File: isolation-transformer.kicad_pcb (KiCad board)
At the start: 2 copper layers, 152.1 x 85.4 mm, 59 parts, among them J1 MODE, J10 PWR, J2 MG950-9.5, J3 MG950-9.5, J4 MG950-9.5, J5 MG950-9.5, J6 MG950-9.5, J7 PWR, J8 MG950-9.5, J9 MG950-9.5, K1 Fujitsu_FTR-F1C, K2 Fujitsu_FTR-F1C, K3 Fujitsu_FTR-F1C, K4 Fujitsu_FTR-F1C, K5 Fujitsu_FTR-F1C, K6 Fujitsu_FTR-F1C, Q1 BC546, Q2 BC546, Q3 BC546, Q4 BC546, Q5 BC546, Q6 BC546, U1 HEF4093B, U2 NE555, U3 LM7805_TO220, U4 7400, U5 NE555, U6 NE555

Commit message: Fixes in mode selection logic
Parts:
- R4: value 4.7k -> 3k
- R7: value 1k -> 10
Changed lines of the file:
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@@
       (effects (font (size 1 1) (thickness 0.15)))
     )
-    (fp_text value 1k (at 1.27 2.37 90) (layer F.Fab)
+    (fp_text value 10 (at 1.27 2.37 90) (layer F.Fab)
       (effects (font (size 1 1) (thickness 0.15)))
     )
@@
       (effects (font (size 1 1) (thickness 0.15)))
     )
-    (fp_text value 4.7k (at 1.27 2.37) (layer F.Fab)
-      (effects (font (size 1 1) (thickness 0.15)))
-    )
+    (fp_text value 3k (at 1.27 2.37) (layer F.Fab)
+      (effects (font (size 1 1) (thickness 0.15)))
+    )

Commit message: Fix relay firing order in soft-start
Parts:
- R11: value 22k -> 10k
- R13: value 10k -> 22k
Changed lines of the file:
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@@
       (effects (font (size 1 1) (thickness 0.15)))
     )
-    (fp_text value 22k (at 1.27 2.37) (layer F.Fab)
+    (fp_text value 10k (at 1.27 2.37) (layer F.Fab)
       (effects (font (size 1 1) (thickness 0.15)))
     )
@@
       (effects (font (size 1 1) (thickness 0.15)))
     )
-    (fp_text value 10k (at 1.27 2.37 180) (layer F.Fab)
+    (fp_text value 22k (at 1.27 2.37 180) (layer F.Fab)
       (effects (font (size 1 1) (thickness 0.15)))
     )

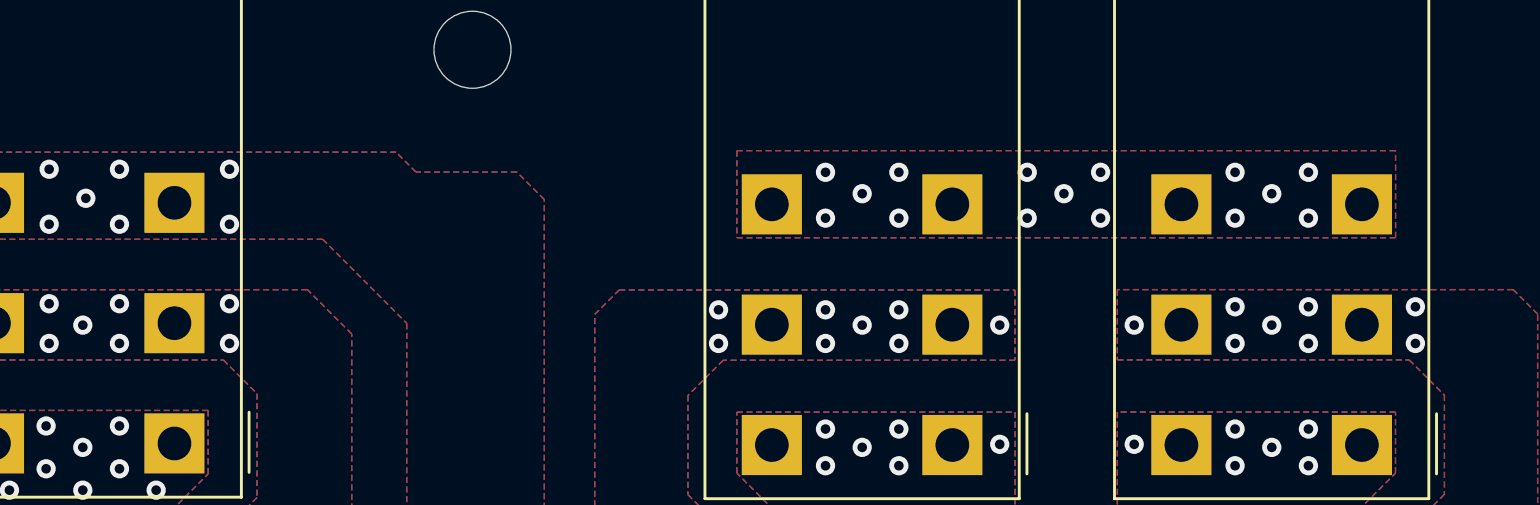
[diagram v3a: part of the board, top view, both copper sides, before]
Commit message: Actually used parts instead of generic ones
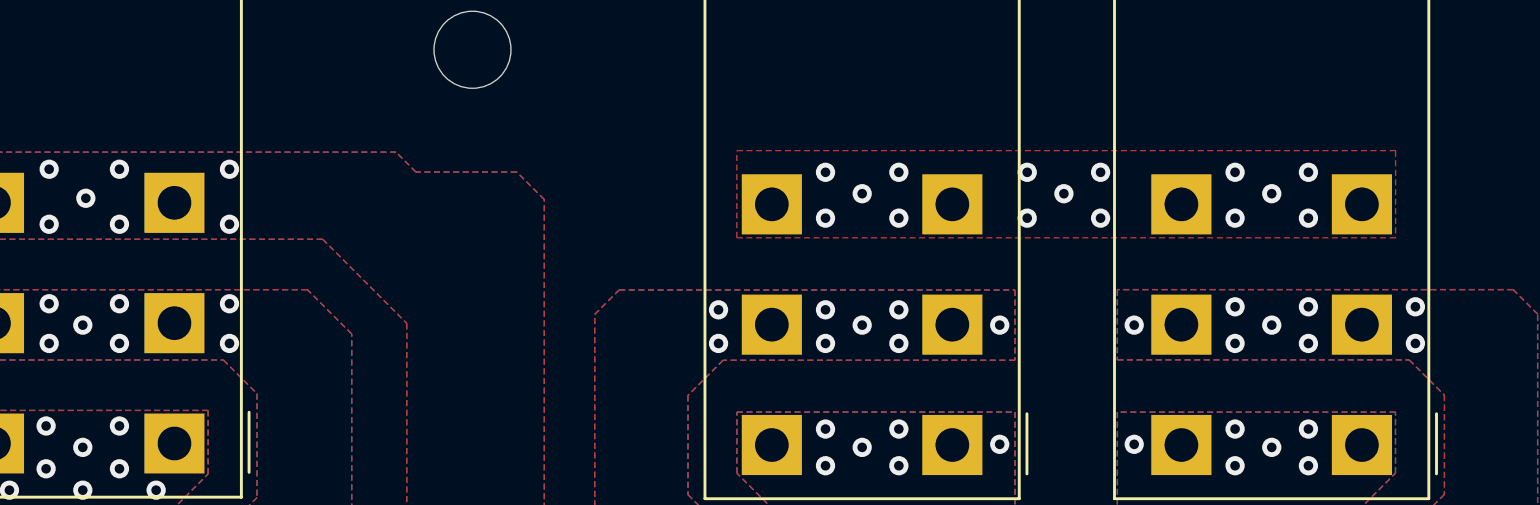
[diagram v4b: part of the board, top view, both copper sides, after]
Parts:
- K1: value Fujitsu_FTR-F1C -> G2R-1-E-12VDC
- K2, K3, K4: value Fujitsu_FTR-F1C -> G2R-1-E-12VDC; footprint Relay_THT:Relay_DPDT_Fujitsu_FTR-F1C -> CustomParts:Relay_SPDT_Omron_G2R-1-E
- K5, K6: value Fujitsu_FTR-F1C -> FTR-K1CK012W
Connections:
- K1 pad 1: /Mode Selection/115V_1_L -> Net-(D1-Pad2)
- K1 pad 2: /Mode Selection/W5 -> /Mode Selection/230V_L
- K1 pad 3: /Mode Selection/230V_L -> /Mode Selection/W5
- K1 pad 4: Net-(D1-Pad2) -> /Mode Selection/115V_1_L
- K1 pad 5: +12V -> /Mode Selection/115V_1_L
- K1 pad 6: /Mode Selection/230V_L -> /Mode Selection/W5
- K1 pad 7: /Mode Selection/W5 -> /Mode Selection/230V_L
- K1 pad 8: /Mode Selection/115V_1_L -> +12V
- K2 pad 1: /Mode Selection/115V_1_N -> Net-(D2-Pad2)
- K2 pad 2: /Mode Selection/W6 -> Net-(K2-Pad2)
- K2 pad 3: Net-(K2-Pad3) -> /Mode Selection/W6
- K2 pad 4: Net-(D2-Pad2) -> /Mode Selection/115V_1_N
- K2 pad 5: +12V -> /Mode Selection/115V_1_N
- K2 pad 6: Net-(K2-Pad3) -> /Mode Selection/W6
- K2 pad 7: /Mode Selection/W6 -> Net-(K2-Pad2)
- K2 pad 8: /Mode Selection/115V_1_N -> +12V
- K3 pad 1: /Mode Selection/115V_2_L -> +12V
- K3 pad 2: /Mode Selection/W7 -> Net-(K2-Pad2)
- K3 pad 3: Net-(K2-Pad3) -> /Mode Selection/W7
- K3 pad 4: +12V -> /Mode Selection/115V_2_L
- K3 pad 5: Net-(D3-Pad2) -> /Mode Selection/115V_2_L
- K3 pad 6: Net-(K2-Pad3) -> /Mode Selection/W7
- K3 pad 7: /Mode Selection/W7 -> Net-(K2-Pad2)
- K3 pad 8: /Mode Selection/115V_2_L -> Net-(D3-Pad2)
- K4 pad 1: /Mode Selection/115V_2_N -> Net-(D4-Pad2)
- K4 pad 2: /Mode Selection/W8 -> /Mode Selection/230V_N
- K4 pad 3: /Mode Selection/230V_N -> /Mode Selection/W8
- K4 pad 4: Net-(D4-Pad2) -> /Mode Selection/115V_2_N
- K4 pad 5: +12V -> /Mode Selection/115V_2_N
- K4 pad 6: /Mode Selection/230V_N -> /Mode Selection/W8
- K4 pad 7: /Mode Selection/W8 -> /Mode Selection/230V_N
- K4 pad 8: /Mode Selection/115V_2_N -> +12V
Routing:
- net Net-(K2-Pad3): vias 15 -> 0
- net Net-(K2-Pad2): vias 0 -> 15
- added copper zone on F.Cu, net Net-(K2-Pad2)
- removed copper zone on B.Cu, net Net-(K2-Pad3)
- removed copper zone on F.Cu, net Net-(K2-Pad3)

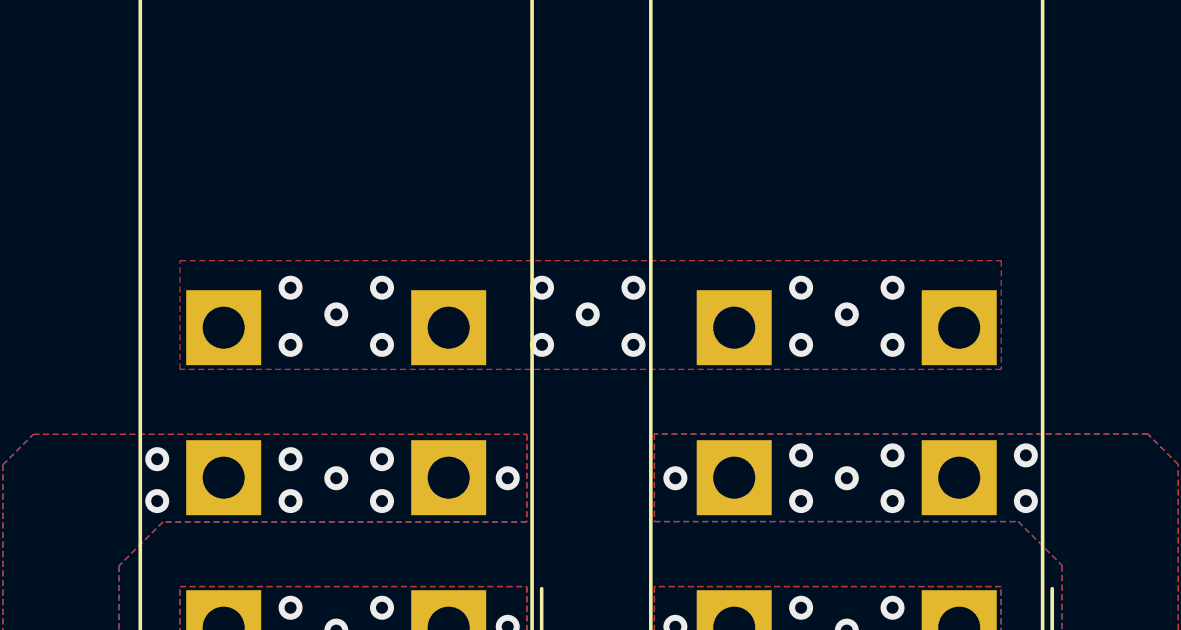
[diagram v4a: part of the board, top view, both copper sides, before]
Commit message: Add PCB photos, fixes in schematics, add lost PCB track
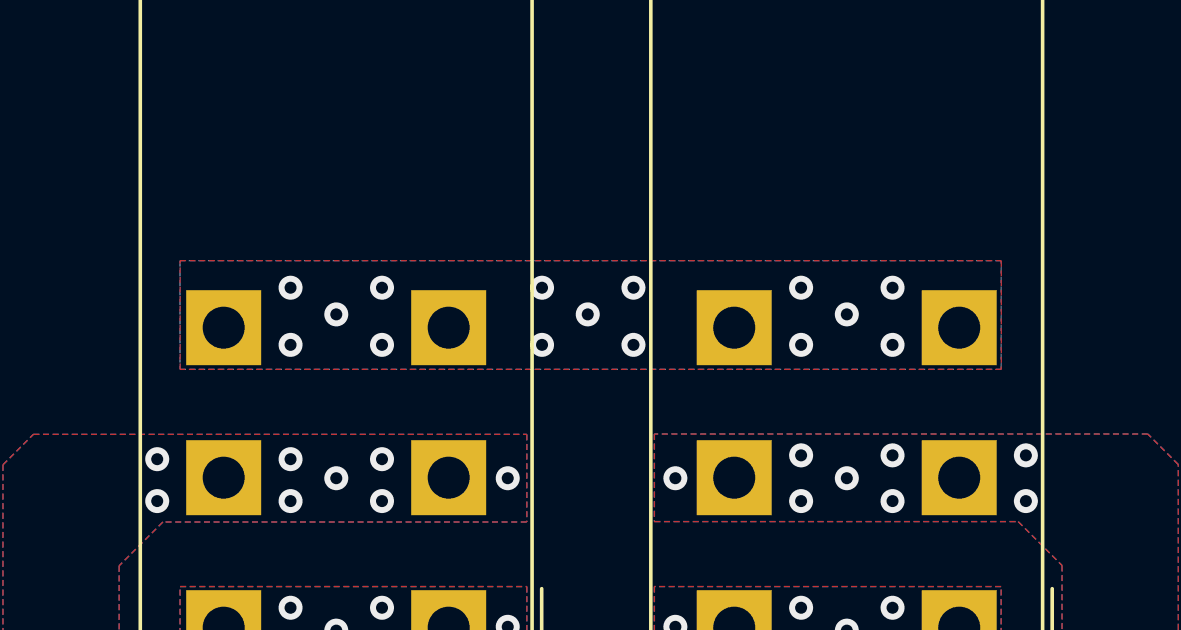
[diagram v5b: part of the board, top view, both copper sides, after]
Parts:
- U3: value LM7805_TO220 -> DD4012SB_5V
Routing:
- added copper zone on B.Cu, net Net-(K2-Pad2)
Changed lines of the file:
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@@
       (effects (font (size 1 1) (thickness 0.15)))
     )
-    (fp_text value LM7805_TO220 (at 2.54 2 90) (layer F.Fab)
+    (fp_text value DD4012SB_5V (at 2.54 2 90) (layer F.Fab)
       (effects (font (size 1 1) (thickness 0.15)))
     )
@@
       )
     )
+  )
+  (zone (net 58) (net_name "Net-(K2-Pad2)") (layer B.Cu) (hatch edge 0.508)
+    (connect_pads yes (clearance 0.508))
+    (min_thickness 0.254)
+    (fill yes (arc_segments 16) (thermal_gap 0.508) (thermal_bridge_width 0.508))
+    (polygon
+      (pts
+        (xy 84.36996 88.2984) (xy 84.3725 88.2984) (xy 84.3725 84.6789) (xy 57.004 84.6789) (xy 57.004 84.68144)
+        (xy 57.00146 84.68144) (xy 57.00146 88.30094) (xy 84.36996 88.30094)
+      )
+    )

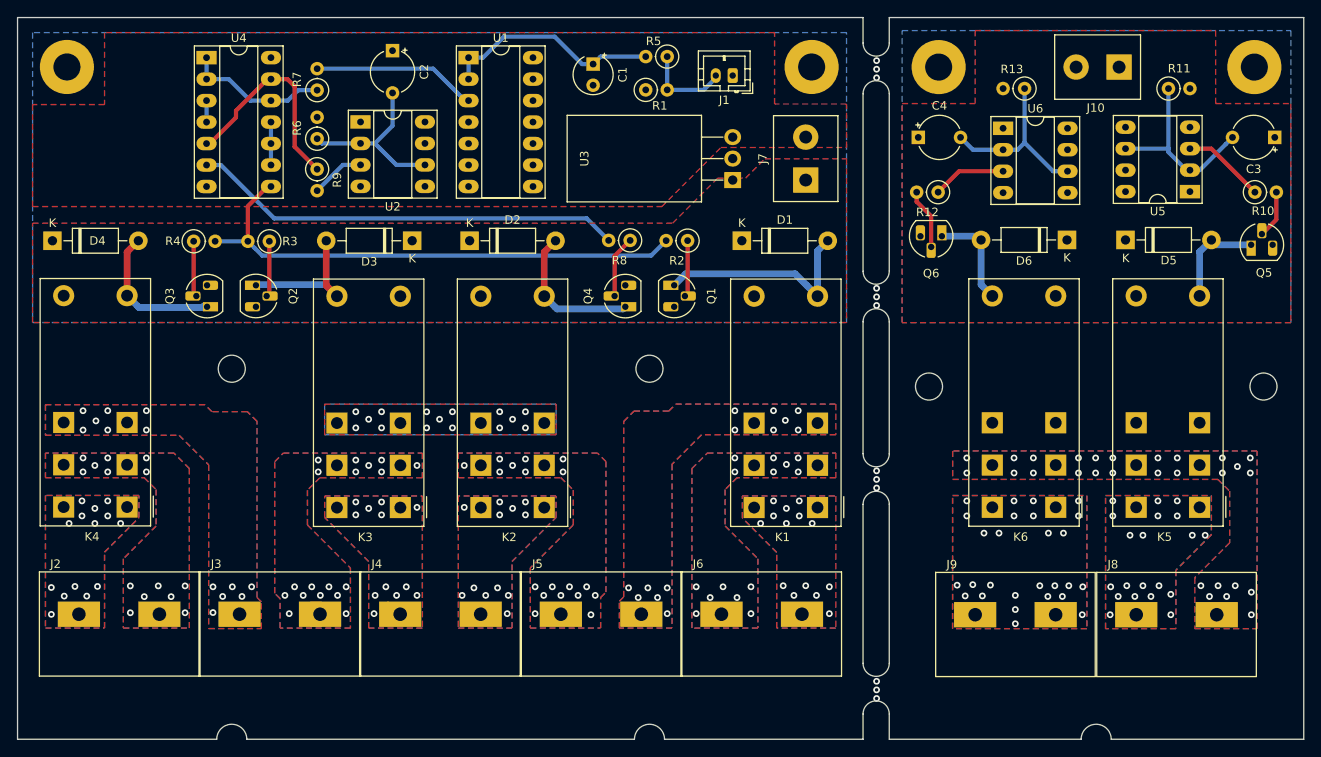
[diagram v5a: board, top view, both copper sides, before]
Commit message: Migrate to KiCad 6
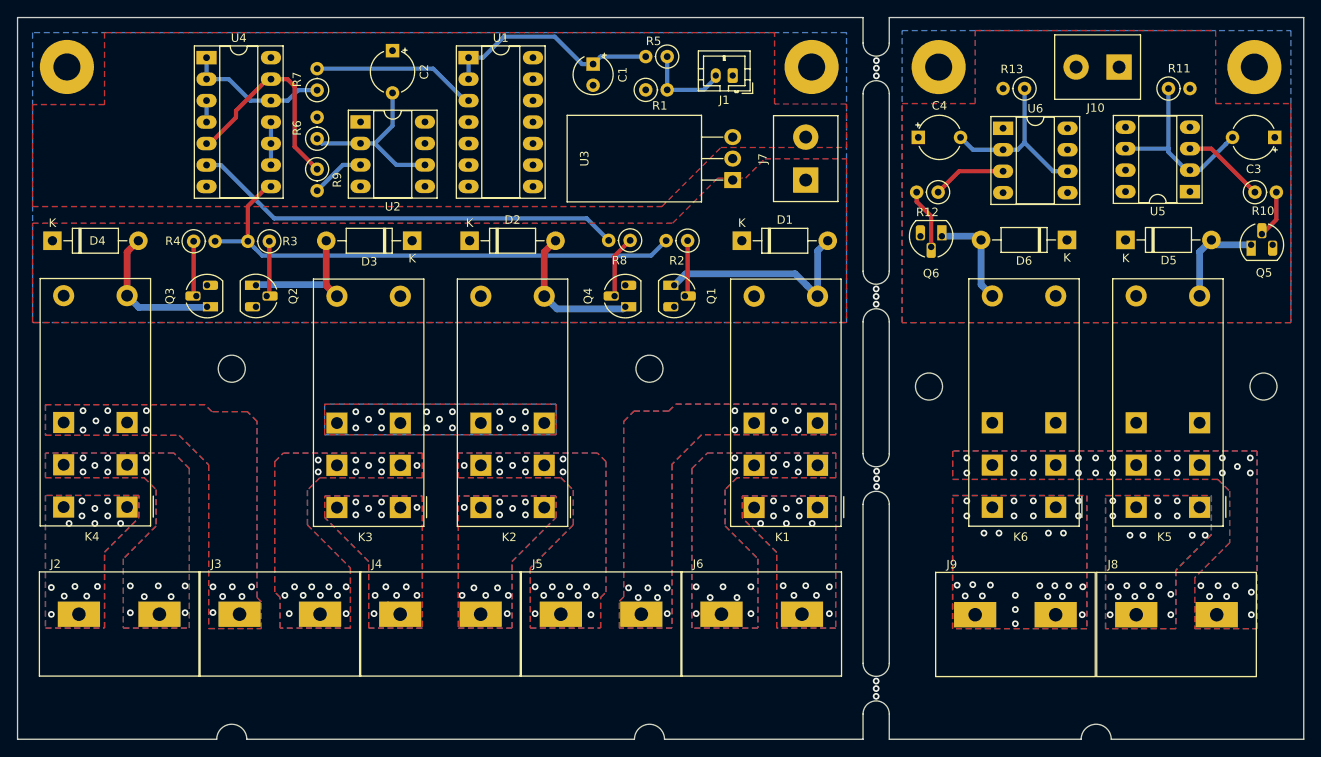
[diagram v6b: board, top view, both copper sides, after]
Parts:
- K1: footprint Relay_THT:Relay_DPDT_Fujitsu_FTR-F1C -> CustomParts:Relay_SPDT_Omron_G2R-1-E
- K5, K6: footprint Relay_THT:Relay_DPDT_Fujitsu_FTR-F1C -> CustomParts:Relay_SPDT_Fujitsu_FTR-K1C
- MT1, MT2, MT3, MT4, MT5, MT6, MT7, MT8: value Conn_01x01 -> M3
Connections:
- K5 pad 3: Net-(K5-Pad3) -> unconnected-(K5-Pad3)
- K5 pad 6: Net-(K5-Pad6) -> unconnected-(K5-Pad6)
- K6 pad 3: Net-(K6-Pad3) -> unconnected-(K6-Pad3)
- K6 pad 6: Net-(K6-Pad6) -> unconnected-(K6-Pad6)
- U1 pad 10: (no net) -> unconnected-(U1-Pad10)
- U1 pad 11: (no net) -> unconnected-(U1-Pad11)
- U1 pad 12: (no net) -> unconnected-(U1-Pad12)
- U1 pad 13: (no net) -> unconnected-(U1-Pad13)
- U1 pad 4: (no net) -> unconnected-(U1-Pad4)
- U1 pad 5: (no net) -> unconnected-(U1-Pad5)
- U1 pad 6: (no net) -> unconnected-(U1-Pad6)
- U1 pad 8: (no net) -> unconnected-(U1-Pad8)
- U1 pad 9: (no net) -> unconnected-(U1-Pad9)
- U2 pad 5: Net-(U2-Pad5) -> unconnected-(U2-Pad5)
- U2 pad 7: Net-(U2-Pad7) -> unconnected-(U2-Pad7)
- U5 pad 5: Net-(U5-Pad5) -> unconnected-(U5-Pad5)
- U5 pad 7: Net-(U5-Pad7) -> unconnected-(U5-Pad7)
- U6 pad 5: Net-(U6-Pad5) -> unconnected-(U6-Pad5)
- U6 pad 7: Net-(U6-Pad7) -> unconnected-(U6-Pad7)
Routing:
- net /Mode Selection/W7: track 1.05 -> 0.00 mm
- net /Mode Selection/115V_1_N: track 1.00 -> 0.00 mm
- net /Mode Selection/W8: track 0.84 -> 0.00 mm
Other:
- net class Default removed
- net class HV removed
- net class LV removed
